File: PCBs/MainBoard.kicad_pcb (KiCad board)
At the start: 2 copper layers, 40.4 x 70 mm, 48 parts, among them J1 USB_C_Receptacle, J2 Conn_01x12_FPC_0.5mm, J3 Conn_01x08, J4 Qwiic_RA, J5 SM06B-GHS-TB, SW1 PTH_RA_h7.5mm, SW2 SMD_4.6x2.8mm_h2.5mm, SW3 SMD_4.6x2.8mm_h2.5mm, U1 TVS_ESD_USB, U2 ESP32-S3-MINI, U3 AP3012, U4 MQ-4 Gas Sensor, U5 PASCO2V01BUMA1, U6 AP2112K-3.3, U7 MQ-7 Gas Sensor

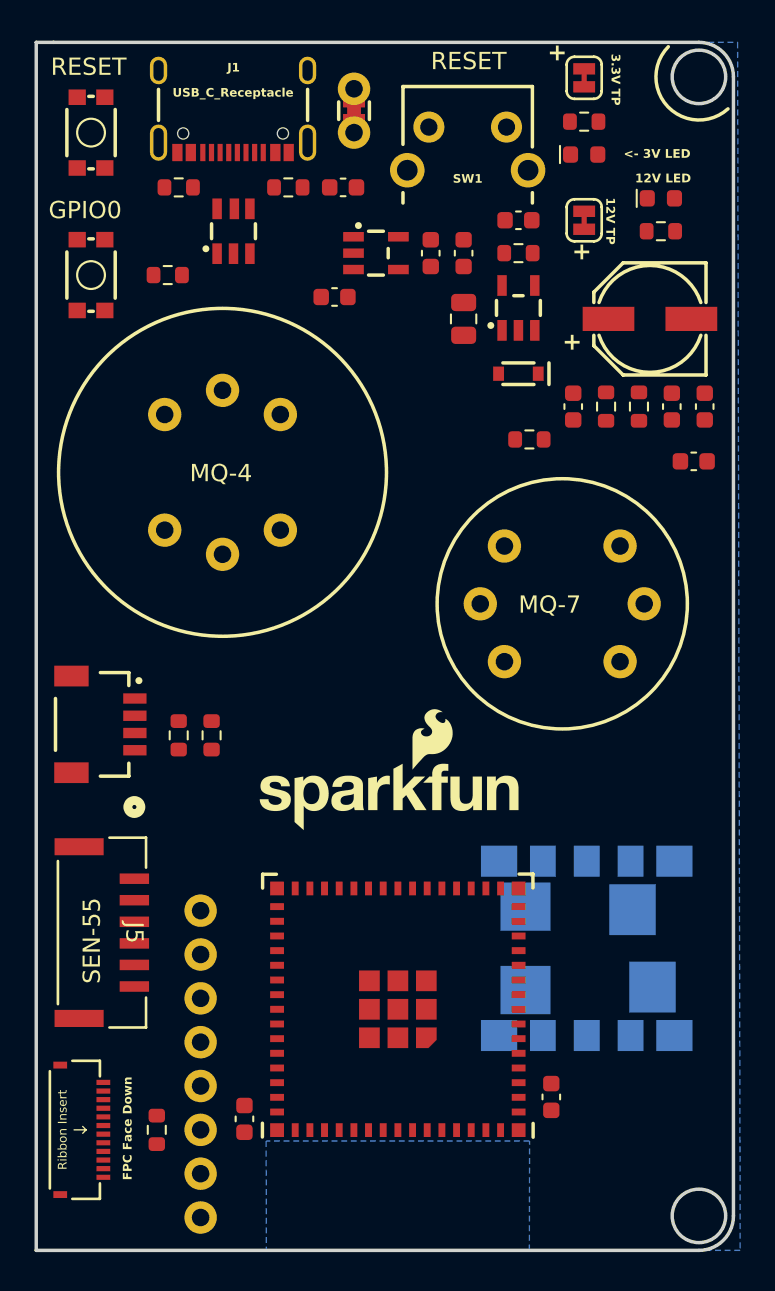
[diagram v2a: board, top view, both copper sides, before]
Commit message: Making updates
Making updates from Board Review Google doc
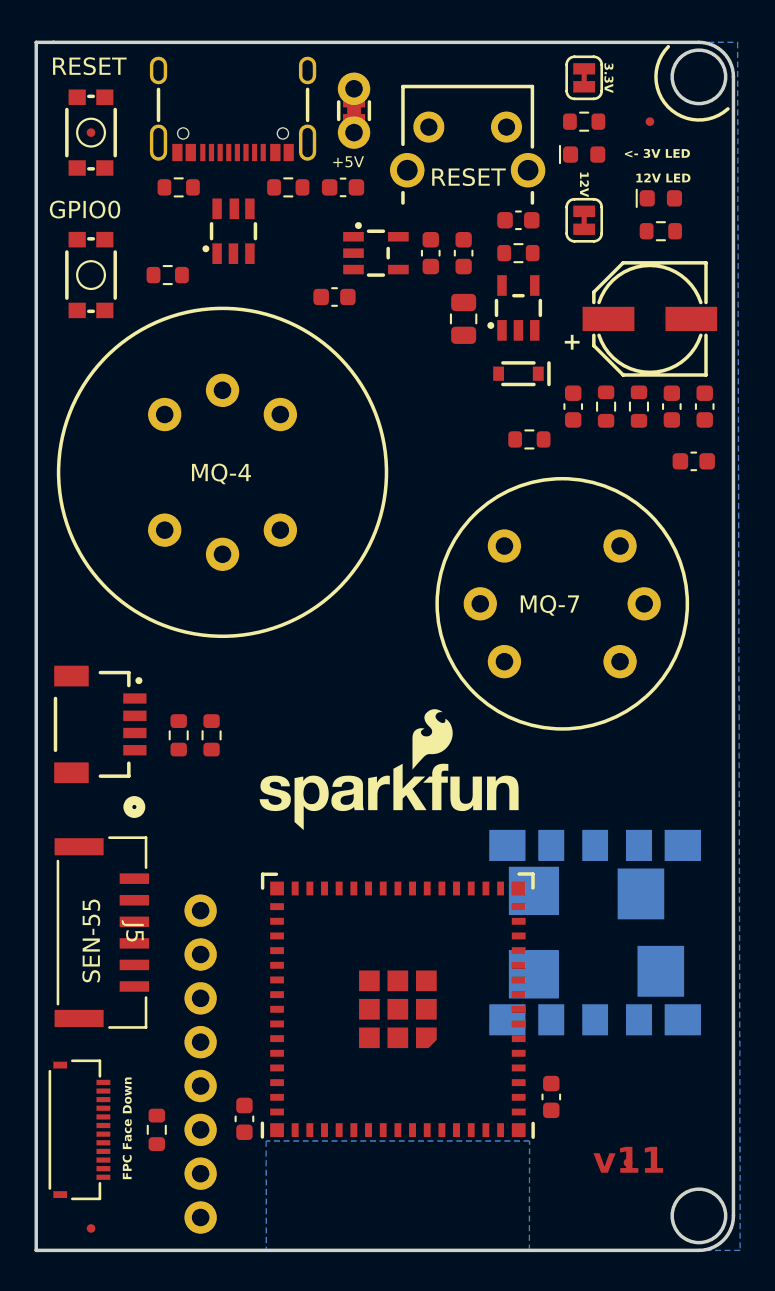
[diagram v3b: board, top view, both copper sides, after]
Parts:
- added Ref**: Fiducial_0.5mm_Mask1mm, SparkFun-Aesthetic:Fiducial_0.5mm_Mask1mm, F.Cu at (132.0, 59.1)
- added Ref**: Fiducial_0.5mm_Mask1mm, SparkFun-Aesthetic:Fiducial_0.5mm_Mask1mm, F.Cu at (163.1, 118.8)
- added Ref**: Fiducial_0.5mm_Mask1mm, SparkFun-Aesthetic:Fiducial_0.5mm_Mask1mm, F.Cu at (164.4, 58.5)
- added Ref**: Fiducial_0.5mm_Mask1mm, SparkFun-Aesthetic:Fiducial_0.5mm_Mask1mm, F.Cu at (132.0, 122.6)
- moved U5 1.04 mm to (161.2, 105.5)
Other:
- board text added: "+5V"
- board text added: "12V"
- board text added: "3.3V"
- board text added: "SparkFun Home Air Quality Monitor Main Enclosure PCB V11 Capstone F23 - The Band Author: Anton Vandenberge"
- board text added: "v11"
- board text removed: "12V TP"
- board text removed: "3.3V TP"
- board text removed: "SparkFun Home Air Quality Monitor Main Enclosure PCB V1.2 Capstone F23 - The Band Author: Anton Vandenberge"
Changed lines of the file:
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@@
     )
   )
+  (footprint "SparkFun-Aesthetic:Fiducial_0.5mm_Mask1mm" (layer "F.Cu")
+    (at 131.975 59.13)
+    (descr "Circular Fiducial, 0.5mm bare copper, 1mm soldermask opening (Level C)")
+    (tags "fiducial")
+    (attr smd)
+    (fp_text reference "Ref**" (at 0 -1.5) (layer "F.Fab")
+        (effects (font (size 0.5 0.5) (thickness 0.1)))
+    )
+    (fp_text value "Fiducial_0.5mm_Mask1mm" (at 0 1.5) (layer "F.Fab") hide
+        (effects (font (size 0.5 0.5) (thickness 0.1)))
+    )
+    (fp_circle (center 0 0) (end 0.75 0)
+      (stroke (width 0.05) (type solid)) (fill none) (layer "F.CrtYd"))
+    (fp_circle (center 0 0) (end 0.5 0)
+      (stroke (width 0.1) (type solid)) (fill none) (layer "F.Fab"))
+    (pad "" smd circle (at 0 0) (size 0.5 0.5) (layers "F.Cu" "F.Mask")
+      (solder_mask_margin 0.25) (clearance 0.25))
+  )
   (footprint "SparkFun-Jumper:SMT-JUMPER_2_NC_TRACE_SILK" (layer "F.Cu")
     (at 160.55 64.21 -90)
@@
     (property "ki_keywords" "solder jumper SPST")
     (net_tie_pad_groups "1,2")
-    (fp_text reference "JP2" (at -1.27 0 -180) (layer "F.Fab")
+    (fp_text reference "JP2" (at 1.9304 -0.0508 -180) (layer "F.Fab")
         (effects (font (size 0.5 0.5) (thickness 0.1) bold) (justify bottom))
     )
@@
     )
   )
+  (footprint "SparkFun-Aesthetic:Fiducial_0.5mm_Mask1mm" (layer "F.Cu")
+    (at 163.09 118.82)
+    (descr "Circular Fiducial, 0.5mm bare copper, 1mm soldermask opening (Level C)")
+    (tags "fiducial")
+    (attr smd)
+    (fp_text reference "Ref**" (at 0 -1.5) (layer "F.Fab")
+        (effects (font (size 0.5 0.5) (thickness 0.1)))
+    )
+    (fp_text value "Fiducial_0.5mm_Mask1mm" (at 0 1.5) (layer "F.Fab") hide
+        (effects (font (size 0.5 0.5) (thickness 0.1)))
+    )
+    (fp_circle (center 0 0) (end 0.75 0)
+      (stroke (width 0.05) (type solid)) (fill none) (layer "F.CrtYd"))
+    (fp_circle (center 0 0) (end 0.5 0)
+      (stroke (width 0.1) (type solid)) (fill none) (layer "F.Fab"))
+    (pad "" smd circle (at 0 0) (size 0.5 0.5) (layers "F.Cu" "F.Mask")
+      (solder_mask_margin 0.25) (clearance 0.25))
+  )
   (footprint "SparkFun-Resistor:R_0603_1608Metric" (layer "F.Cu")
     (at 143.405 62.305)
@@
     (property "ki_description" "Single Pole Single Throw (SPST) switch")
     (property "ki_keywords" "switch lever")
-    (fp_text reference "SW1" (at 0 -3.285) (layer "F.SilkS")
+    (fp_text reference "SW1" (at 0 -0.066) (layer "F.Fab")
         (effects (font (size 0.5 0.5) (thickness 0.1) bold) (justify bottom))
     )
@@
     )
   )
+  (footprint "SparkFun-Aesthetic:Fiducial_0.5mm_Mask1mm" (layer "F.Cu")
+    (at 164.36 58.495)
+    (descr "Circular Fiducial, 0.5mm bare copper, 1mm soldermask opening (Level C)")
+    (tags "fiducial")
+    (attr smd)
+    (fp_text reference "Ref**" (at 0 -1.5) (layer "F.Fab")
+        (effects (font (size 0.5 0.5) (thickness 0.1)))
+    )
+    (fp_text value "Fiducial_0.5mm_Mask1mm" (at 0 1.5) (layer "F.Fab")
+        (effects (font (size 0.5 0.5) (thickness 0.1)))
+    )
+    (fp_circle (center 0 0) (end 0.75 0)
+      (stroke (width 0.05) (type solid)) (fill none) (layer "F.CrtYd"))
+    (fp_circle (center 0 0) (end 0.5 0)
+      (stroke (width 0.1) (type solid)) (fill none) (layer "F.Fab"))
+    (pad "" smd circle (at 0 0) (size 0.5 0.5) (layers "F.Cu" "F.Mask")
+      (solder_mask_margin 0.25) (clearance 0.25))
+  )
   (footprint "SparkFun-Aesthetic:Creative_Commons_License" (layer "F.Cu")
     (at 116.735 77.545)
@@
     (property "ki_keywords" "solder jumper SPST")
     (net_tie_pad_groups "1,2")
-    (fp_text reference "JP1" (at 0 -1.143 90) (layer "F.Fab")
+    (fp_text reference "JP1" (at 0 -1.7018 90) (layer "F.Fab")
         (effects (font (size 0.5 0.5) (thickness 0.1) bold) (justify bottom))
     )
-    (fp_text value "Measure" (at 0 1.143 90) (layer "F.Fab")
+    (fp_text value "Measure" (at -0.0508 1.8034 90) (layer "F.Fab")
         (effects (font (size 0.5 0.5) (thickness 0.1) bold) (justify top))
     )
@@
     (property "ki_description" "USB 2.0-only Type-C Receptacle connector")
     (property "ki_keywords" "usb universal serial bus type-C USB2.0")
-    (fp_text reference "J1" (at -0.03 5.264) (layer "F.SilkS")
+    (fp_text reference "J1" (at -0.03 5.264) (layer "F.Fab")
         (effects (font (size 0.5 0.5) (thickness 0.1) bold))
     )
-    (fp_text value "USB_C_Receptacle" (at 0 3.81) (layer "F.SilkS")
+    (fp_text value "USB_C_Receptacle" (at 0 3.81) (layer "F.Fab")
         (effects (font (size 0.5 0.5) (thickness 0.1) bold))
     )
@@
     )
   )
+  (footprint "SparkFun-Aesthetic:Fiducial_0.5mm_Mask1mm" (layer "F.Cu")
+    (at 131.975 122.63)
+    (descr "Circular Fiducial, 0.5mm bare copper, 1mm soldermask opening (Level C)")
+    (tags "fiducial")
+    (attr smd)
+    (fp_text reference "Ref**" (at -1.905 0) (layer "F.Fab")
+        (effects (font (size 0.5 0.5) (thickness 0.1)))
+    )
+    (fp_text value "Fiducial_0.5mm_Mask1mm" (at 0 1.5) (layer "F.Fab") hide
+        (effects (font (size 0.5 0.5) (thickness 0.1)))
+    )
+    (fp_circle (center 0 0) (end 0.75 0)
+      (stroke (width 0.05) (type solid)) (fill none) (layer "F.CrtYd"))
+    (fp_circle (center 0 0) (end 0.5 0)
+      (stroke (width 0.1) (type solid)) (fill none) (layer "F.Fab"))
+    (pad "" smd circle (at 0 0) (size 0.5 0.5) (layers "F.Cu" "F.Mask")
+      (solder_mask_margin 0.25) (clearance 0.25))
+  )
   (footprint "SparkFun-Connector:FPC_12_0.5MM" (layer "F.Cu")
     (at 131.34 116.915 -90)
@@
         (effects (font (size 0.5 0.5) (thickness 0.1) bold))
     )
-    (fp_text user "Ribbon Insert" (at 0 1.016 90) (layer "F.SilkS")
+    (fp_text user "Ribbon Insert" (at 0 1.016 90) (layer "F.Fab")
         (effects (font (size 0.508 0.508) (thickness 0.1016)))
     )
@@
     (fp_line (start -3.4 1.75) (end 3.4 1.75)
       (stroke (width 0.1524) (type solid)) (layer "F.SilkS"))
-    (fp_line (start 0 -0.35) (end -0.2 -0.15)
-      (stroke (width 0.05) (type solid)) (layer "F.SilkS"))
-    (fp_line (start 0 -0.35) (end 0.2 -0.15)
-      (stroke (width 0.05) (type solid)) (layer "F.SilkS"))
-    (fp_line (start 0 0.35) (end 0 -0.35)
-      (stroke (width 0.05) (type solid)) (layer "F.SilkS"))
     (fp_line (start 4 -1.15) (end 3.1 -1.15)
       (stroke (width 0.1524) (type solid)) (layer "F.SilkS"))
@@
     (fp_line (start -3.62 1.55) (end -3.62 0.75)
       (stroke (width 0.01) (type solid)) (layer "F.Fab"))
+    (fp_line (start 0 -0.35) (end -0.2 -0.15)
+      (stroke (width 0.05) (type solid)) (layer "F.Fab"))
+    (fp_line (start 0 -0.35) (end 0.2 -0.15)
+      (stroke (width 0.05) (type solid)) (layer "F.Fab"))
+    (fp_line (start 0 0.35) (end 0 -0.35)
+      (stroke (width 0.05) (type solid)) (layer "F.Fab"))
     (fp_line (start 3.41 1.75) (end -3.41 1.75)
       (stroke (width 0.01) (type solid)) (layer "F.Fab"))
@@
   )
   (footprint "SparkFun-Sensor:LG-MLGA-14-1_Z8B00206105" (layer "B.Cu")
-    (at 160.7 106.4 180)
+    (at 161.185 105.485 180)
     (property "PROD_ID" "IC-19132")
     (property "Sheetfile" "MainBoard.kicad_sch")
@@
   (gr_circle (center 167.2 121.9) (end 168.75 121.9)
     (stroke (width 0.2) (type default)) (fill none) (layer "Edge.Cuts"))
-  (gr_text "SparkFun Home Air Quality Monitor \nMain Enclosure PCB V1.2\nCapstone F23 - The Band\nAuthor: Anton Vandenberge" (at 148.0786 91.5658 90) (layer "B.SilkS")
+  (gr_text "v11" (at 161.058 119.582) (layer "F.Cu")
+    (effects (font (size 1.5 1.5) (thickness 0.3) bold) (justify left bottom))
+  )
+  (gr_text "SparkFun Home Air Quality Monitor \nMain Enclosure PCB V11\nCapstone F23 - The Band\nAuthor: Anton Vandenberge" (at 148.0786 91.5658 90) (layer "B.SilkS")
     (effects (font (size 1.5 1.5) (thickness 0.3) bold) (justify mirror))
   )
@@
     (effects (font (size 1 1) (thickness 0.15)) (justify left bottom))
   )
+  (gr_text "+5V" (at 145.9196 61.2128) (layer "F.SilkS")
+    (effects (font (size 0.635 0.635) (thickness 0.1016)) (justify left bottom))
+  )
   (gr_text "RESET" (at 129.6382 55.9042) (layer "F.SilkS")
     (effects (font (size 1 1) (thickness 0.15)) (justify left bottom))
@@
     (effects (font (size 0.508 0.508) (thickness 0.1016) bold) (justify left bottom))
   )
-  (gr_text "RESET" (at 151.66 55.574) (layer "F.SilkS")
+  (gr_text "RESET" (at 151.6092 62.3304) (layer "F.SilkS")
     (effects (font (size 1 1) (thickness 0.15)) (justify left bottom))
   )
@@
     (effects (font (size 1 1) (thickness 0.15)) (justify left bottom))
   )
-  (gr_text "12V TP" (at 161.7692 62.8892 -90) (layer "F.SilkS")
+  (gr_text "12V" (at 160.2452 61.3652 270) (layer "F.SilkS" knockout)
     (effects (font (size 0.508 0.508) (thickness 0.1016) bold) (justify left bottom))
   )
@@
     (effects (font (size 1 1) (thickness 0.15)) (justify left bottom))
   )
-  (gr_text "+" (at 159.8388 66.5976) (layer "F.SilkS")
-    (effects (font (size 1 1) (thickness 0.2) bold) (justify left bottom))
-  )
   (gr_text "SEN-55" (at 132.61 108.4568 90) (layer "F.SilkS")
     (effects (font (size 1 1) (thickness 0.15)) (justify left bottom))
   )
-  (gr_text "3.3V TP" (at 162.074 54.558 -90) (layer "F.SilkS")
+  (gr_text "3.3V" (at 161.6676 55.066 270) (layer "F.SilkS" knockout)
     (effects (font (size 0.508 0.508) (thickness 0.1016) bold) (justify left bottom))
   )
-  (gr_text "+" (at 158.4164 55.066) (layer "F.SilkS")
-    (effects (font (size 1 1) (thickness 0.2) bold) (justify left bottom))
-  )
   (zone (net 1) (net_name "GND") (layer "B.Cu") (hatch edge 0.5)

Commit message: fuck you
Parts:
- removed J5: SM06B-GHS-TB, SM06B-GHS-TB:CONN_SM06B-GHS-TB_JST
- removed the Ref** at (132.0, 59.1)
- removed the Ref** at (163.1, 118.8)
- removed the Ref** at (164.4, 58.5)
- removed the Ref** at (132.0, 122.6)
- added FID1: Fiducial_0.5mm, SparkFun-Aesthetic:Fiducial_0.5mm_Mask1mm, F.Cu at (164.4, 120.7)
- added FID2: Fiducial_0.5mm, SparkFun-Aesthetic:Fiducial_0.5mm_Mask1mm, F.Cu at (132.0, 59.1)
- added FID3: Fiducial_0.5mm, SparkFun-Aesthetic:Fiducial_0.5mm_Mask1mm, F.Cu at (164.4, 58.5)
- added FID4: Fiducial_0.5mm, SparkFun-Aesthetic:Fiducial_0.5mm_Mask1mm, F.Cu at (131.3, 122.6)
- added Ref**: Val**, SparkFun-Aesthetic:OSHW_Logo_6mm, B.Cu at (164.9, 117.5)
- added ST1: Stand_off, SparkFun-Hardware:STAND-OFF, F.Cu at (167.2, 55.9)
- added U8: SEN55, SparkFun-Connector:JST-6-SMD-1.25MM-LOCKING, F.Cu at (131.3, 105.5)
- added kibuzzard-65B1D3B2: G***, kibuzzard-65B1D3B2, F.Cu at (159.5, 70.4)
- added kibuzzard-65B1D56F: G***, kibuzzard-65B1D56F, F.Cu at (132.0, 55.4)
- added kibuzzard-65B1D57E: G***, kibuzzard-65B1D57E, F.Cu at (132.0, 63.6)
- added kibuzzard-65B1D5D4: G***, kibuzzard-65B1D5D4, F.Cu at (141.9, 78.7)
- added kibuzzard-65B1D5EA: G***, kibuzzard-65B1D5EA, F.Cu at (159.2, 86.3)
- added kibuzzard-65B1D64A: G***, kibuzzard-65B1D64A, F.Cu at (153.8, 61.7)
- added kibuzzard-65B1D673: G***, kibuzzard-65B1D673, B.Cu at (147.2, 61.0)
- added kibuzzard-65B1DFAF: G***, kibuzzard-65B1DFAF, B.Cu at (167.8, 105.1)
- added kibuzzard-65B1E10A: G***, kibuzzard-65B1E10A, B.Cu at (135.4, 104.1)
- added kibuzzard-65B1E11D: G***, kibuzzard-65B1E11D, B.Cu at (135.4, 106.8)
- added kibuzzard-65B1E12C: G***, kibuzzard-65B1E12C, B.Cu at (135.7, 109.4)
- added kibuzzard-65B1E13C: G***, kibuzzard-65B1E13C, B.Cu at (136.0, 111.8)
- added kibuzzard-65B1E14E: G***, kibuzzard-65B1E14E, B.Cu at (135.2, 114.5)
- added kibuzzard-65B1E160: G***, kibuzzard-65B1E160, B.Cu at (135.5, 116.8)
- added kibuzzard-65B1E16C: G***, kibuzzard-65B1E16C, B.Cu at (135.5, 119.3)
- added kibuzzard-65B1E179: G***, kibuzzard-65B1E179, B.Cu at (135.3, 122.0)
- added kibuzzard-65B1E2D2: G***, kibuzzard-65B1E2D2, F.Cu at (165.0, 61.7)
- added kibuzzard-65B1E2FB: G***, kibuzzard-65B1E2FB, F.Cu at (164.4, 60.4)
- added kibuzzard-65B1E40B: G***, kibuzzard-65B1E40B, F.Cu at (130.3, 116.9)
- added kibuzzard-65B1E438: G***, kibuzzard-65B1E438, B.Cu at (148.9, 82.5)
- added kibuzzard-65B27CA0: G***, kibuzzard-65B27CA0, F.Cu at (129.6, 105.4)
- moved C9 18.6 mm to (164.4, 96.6)
- moved R11 5.68 mm to (152.3, 79.5)
- moved R10 1.91 mm to (139.0, 94.1)
- moved R8 1.91 mm to (137.1, 94.1)
- moved R3 1.90 mm to (135.8, 118.8), turned to 90 degrees
- moved U1 1.42 mm to (141.5, 65.5), turned to 180 degrees
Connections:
- C7 pad +: +12V -> (no net)
- C7 pad -: GND -> (no net)
- J2 pad 3: SCLK -> ~{RST}
- J2 pad 4: SDIO -> D/~{C}
- J2 pad 6: D/~{C} -> SCLK
- J2 pad 7: ~{RST} -> SDIO
- J3 pad 3: SCLK -> ~{RST}
- J3 pad 4: SDIO -> D/~{C}
- J3 pad 6: D/~{C} -> SCLK
- J3 pad 7: ~{RST} -> SDIO
- U2 pad 35: SCLK -> ~{RST}
- U2 pad 36: SDIO -> D/~{C}
- U2 pad 38: D/~{C} -> SCLK
- U2 pad 39: ~{RST} -> SDIO
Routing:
- net +3.3V: track 0.00 -> 165.8 mm, vias 0 -> 2
- net GND: track 0.00 -> 97.6 mm, vias 0 -> 43
- net RESET: track 0.00 -> 94.4 mm, vias 0 -> 2
- net +5V: track 0.00 -> 86.9 mm
- net SCL: track 0.00 -> 68.9 mm, vias 0 -> 3
- net ESP0: track 0.00 -> 58.9 mm, vias 0 -> 2
- net ESP11/MQ4: track 0.00 -> 55.7 mm, vias 0 -> 4
- net +12V: track 0.00 -> 54.3 mm, vias 0 -> 1
- net D-: track 0.00 -> 51.7 mm, vias 0 -> 2
- net D+: track 0.00 -> 50.7 mm, vias 0 -> 2
- net ~{SHDN}-EN: track 0.00 -> 48.5 mm, vias 0 -> 2
- net SDA: track 0.00 -> 45.8 mm, vias 0 -> 3
- net ESP10/MQ7: track 0.00 -> 36.6 mm
- net SDIO: track 0.00 -> 21.2 mm, vias 0 -> 2
- net ~{BUSY}: track 0.00 -> 15.1 mm
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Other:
- board text added: "v11.2"
- board text removed: "+"
- board text removed: "+5V"
- board text removed: "12V LED"
- board text removed: "<- 3V LED"
- board text removed: "FPC Face Down"
- board text removed: "GPIO0"
- board text removed: "MQ-4"
- board text removed: "MQ-7"
- board text removed: "RESET"
- board text removed: "SEN-55"
- board text removed: "SparkFun Home Air Quality Monitor Main Enclosure PCB V11 Capstone F23 - The Band Author: Anton Vandenberge"
- board text removed: "v11"
